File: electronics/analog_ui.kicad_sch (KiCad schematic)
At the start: 21 parts, among them J25 Conn_01x08, SW1 SW_Push, SW2 SW_Push, SW3 SW_Push, SW4 SW_Push, SW5 SW_Push

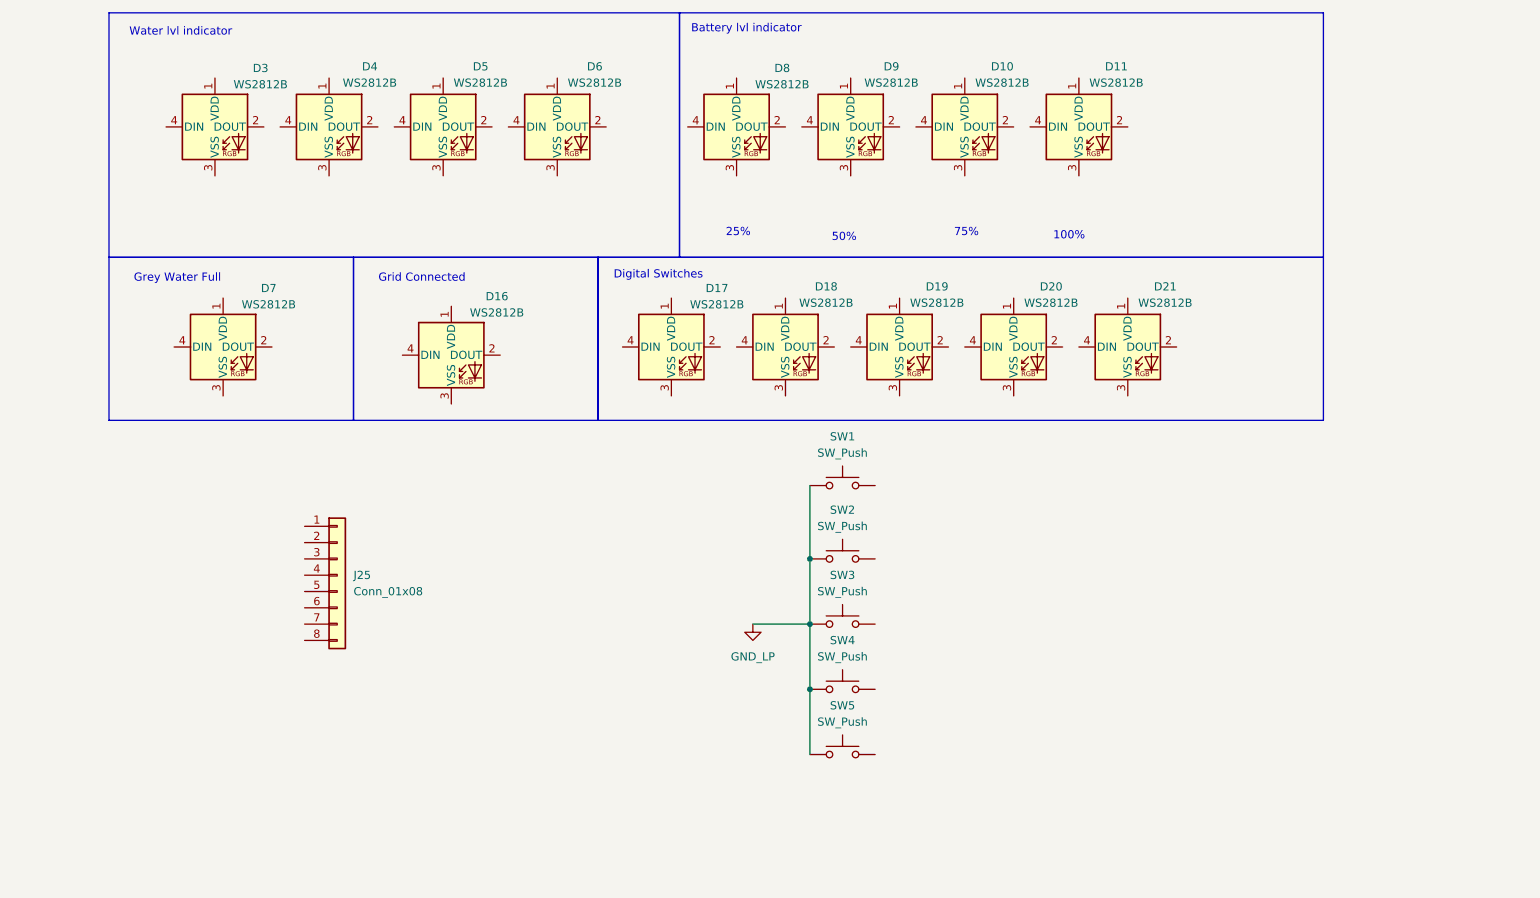
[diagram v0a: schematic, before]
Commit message: capacitors added. universal dc/dc converters
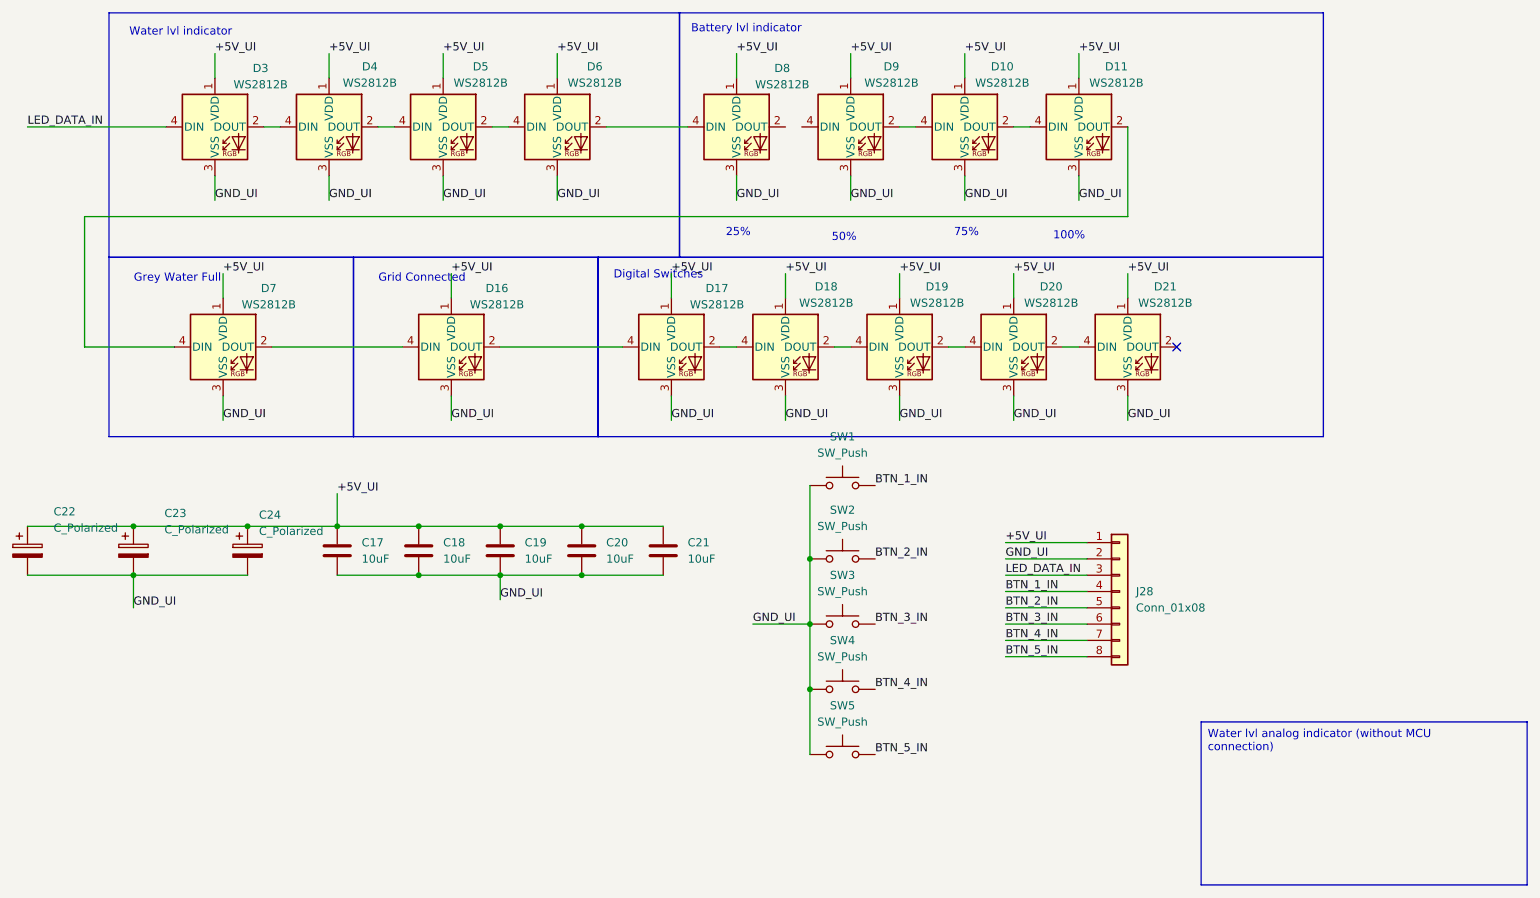
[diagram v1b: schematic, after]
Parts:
- removed J25: Conn_01x08, TerminalBlock:TerminalBlock_Xinya_XY308-2.54-8P_1x08_P2.54mm_Horizontal, symbol Connector_Generic:Conn_01x08
- added C17, C18, C19, C20, C21: 10uF, Capacitor_SMD:C_0805_2012Metric, symbol Device:C
- added C22, C23, C24: C_Polarized, Capacitor_THT:CP_Radial_D5.0mm_P2.50mm, symbol Device:C_Polarized
- added J28: Conn_01x08, TerminalBlock:TerminalBlock_Xinya_XY308-2.54-8P_1x08_P2.54mm_Horizontal, symbol Connector_Generic:Conn_01x08
- D10, D11, D16, D17, D18, D19, D20, D21, D3, D4, D5, D6, D7, D8, D9: footprint LED_SMD:LED_WS2812B-Mini_PLCC4_3.5x3.5mm -> LED_SMD:LED_WS2812B_PLCC4_5.0x5.0mm_P3.2mm
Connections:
- net GND_LP is gone; now on net GND_UI: SW1.1, SW2.1, SW3.1, SW4.1, SW5.1
- net +5V_UI: now reaches D18.1 (VDD)
- net +5V_UI: now also D10.1 (VDD), D11.1 (VDD), D16.1 (VDD), D17.1 (VDD), D19.1 (VDD), D20.1 (VDD), D21.1 (VDD), D3.1 (VDD), D4.1 (VDD), D5.1 (VDD), D6.1 (VDD), D7.1 (VDD), D8.1 (VDD), D9.1 (VDD), C17.1, C18.1, C19.1, C20.1, C21.1, C22.1, C23.1, C24.1, J28.1 (Pin_1)
- net at D18.2 (DOUT): now also D19.4 (DIN)
- net GND_UI: now reaches D18.3 (VSS)
- net GND_UI: now also D10.3 (VSS), D11.3 (VSS), D16.3 (VSS), D17.3 (VSS), D19.3 (VSS), D20.3 (VSS), D21.3 (VSS), D3.3 (VSS), D4.3 (VSS), D5.3 (VSS), D6.3 (VSS), D7.3 (VSS), D8.3 (VSS), D9.3 (VSS), C17.2, C18.2, C19.2, C20.2, C21.2, C22.2, C23.2, C24.2, J28.2 (Pin_2)
- net at D18.4 (DIN): now also D17.2 (DOUT)
- net at D20.2 (DOUT): now also D21.4 (DIN)
- net at D20.4 (DIN): now also D19.2 (DOUT)
- net at D3.2 (DOUT): now also D4.4 (DIN)
- net LED_DATA_IN: now reaches D3.4 (DIN)
- net LED_DATA_IN: now also J28.3 (Pin_3)
- net at D5.2 (DOUT): now also D6.4 (DIN)
- net at D5.4 (DIN): now also D4.2 (DOUT)
- net at D10.2 (DOUT): now also D11.4 (DIN)
- net at D10.4 (DIN): now also D9.2 (DOUT)
- net at D17.4 (DIN): now also D16.2 (DOUT)
- net BTN_3_IN: now reaches SW3.2
- net BTN_3_IN: now also J28.6 (Pin_6)
- net at D8.4 (DIN): now also D6.2 (DOUT)
- net BTN_1_IN: now reaches SW1.2
- net BTN_1_IN: now also J28.4 (Pin_4)
- net BTN_5_IN: now reaches SW5.2
- net BTN_5_IN: now also J28.8 (Pin_8)
- net at D7.2 (DOUT): now also D16.4 (DIN)
- net at D7.4 (DIN): now also D11.2 (DOUT)
- net BTN_4_IN: now reaches SW4.2
- net BTN_4_IN: now also J28.7 (Pin_7)
- net BTN_2_IN: now reaches SW2.2
- net BTN_2_IN: now also J28.5 (Pin_5)
- no-connect marks 0 -> 1
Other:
- moved on the sheet: D16
